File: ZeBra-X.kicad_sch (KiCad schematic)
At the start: 0 parts

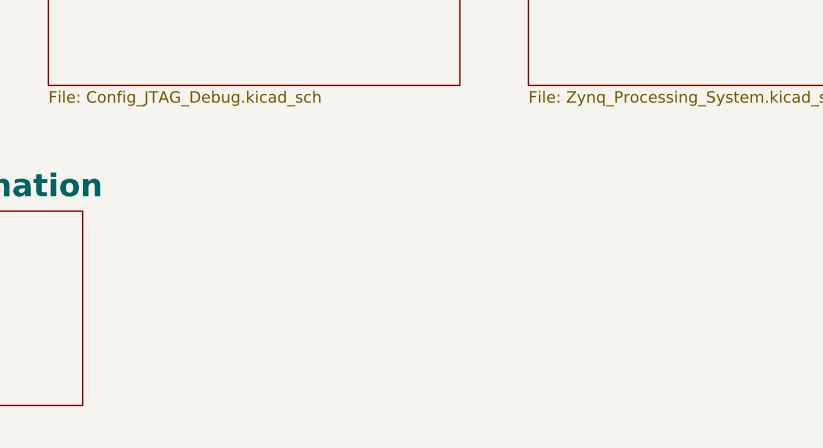
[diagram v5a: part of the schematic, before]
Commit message: Added page '[7] 1GB DDR3L Modules'
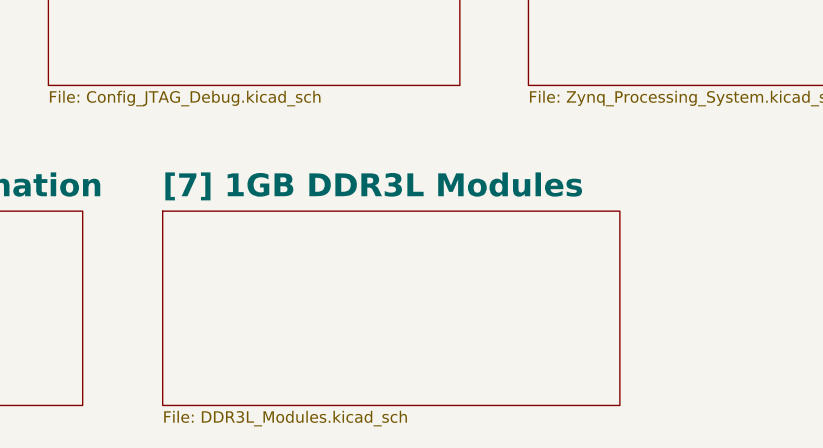
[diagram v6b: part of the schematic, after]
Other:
- added sheet [7] 1GB DDR3L Modules (DDR3L_Modules.kicad_sch)

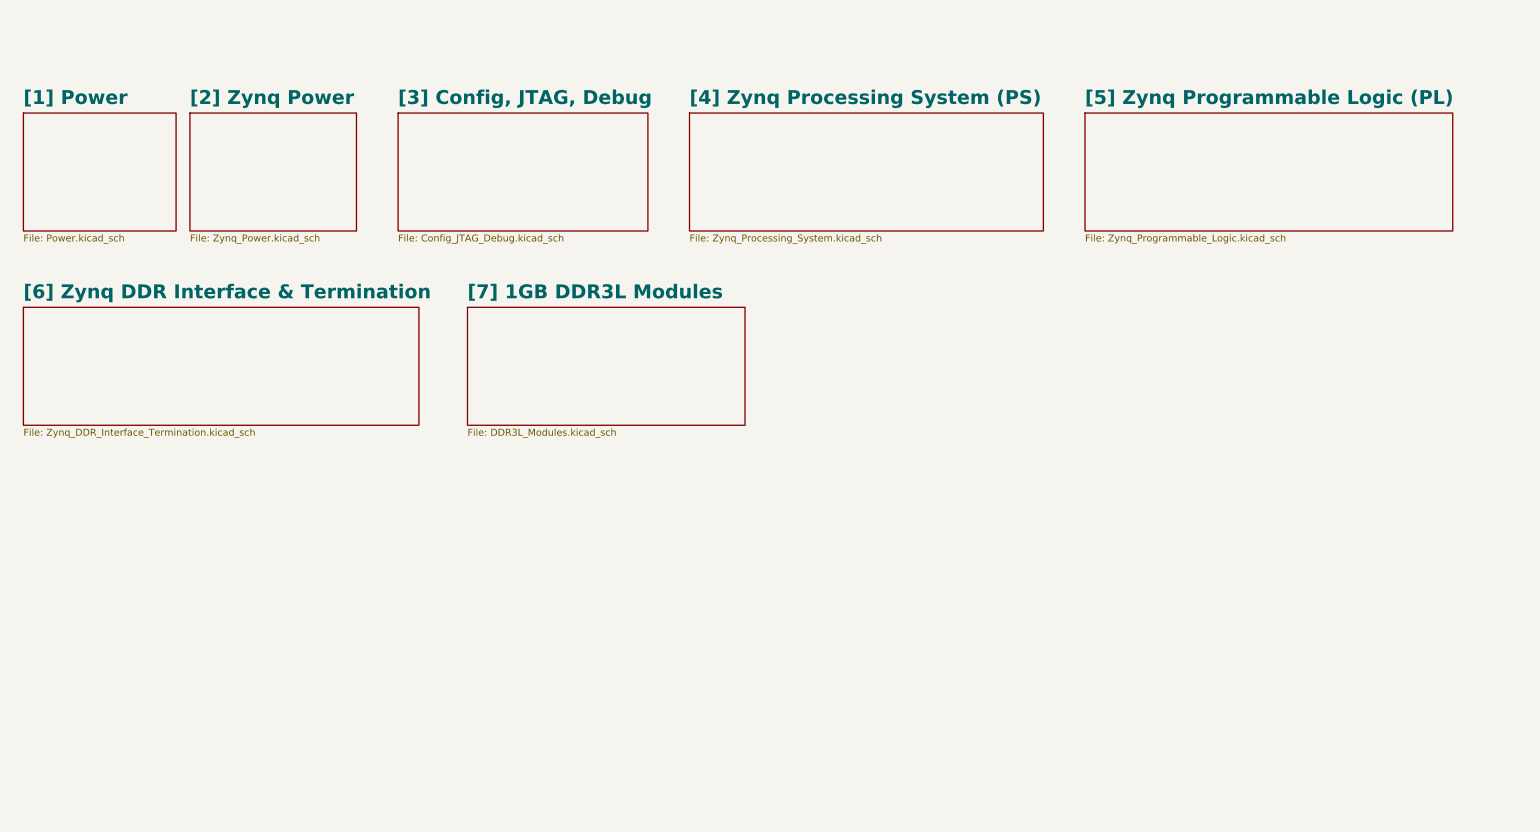
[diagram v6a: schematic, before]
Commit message: Added placeholders for sheets 8,9, and 10
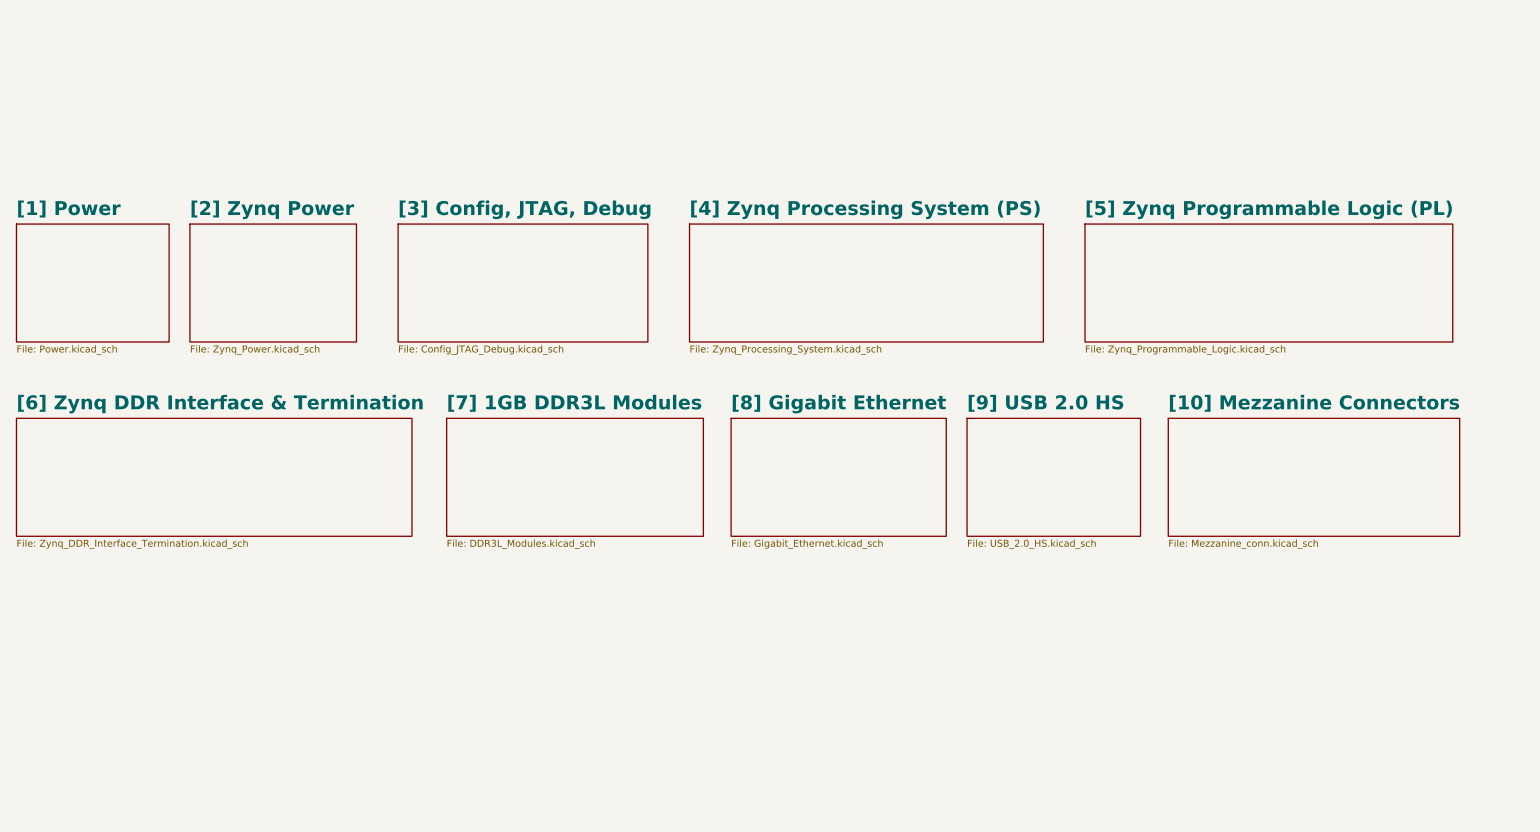
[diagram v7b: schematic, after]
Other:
- added sheet [10] Mezzanine Connectors (Mezzanine_conn.kicad_sch)
- added sheet [8] Gigabit Ethernet (Gigabit_Ethernet.kicad_sch)
- added sheet [9] USB 2.0 HS (USB_2.0_HS.kicad_sch)
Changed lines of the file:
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@@
 	)
 	(sheet
-		(at 138.43 33.02)
+		(at 138.43 53.34)
 		(size 64.77 21.59)
 		(fields_autoplaced yes)
@@
 		)
 		(property "Sheetname" "[4] Zynq Processing System (PS)"
-			(at 138.43 31.6734 0)
+			(at 138.43 51.9934 0)
 			(effects
 				(font
@@
 		)
 		(property "Sheetfile" "Zynq_Processing_System.kicad_sch"
-			(at 138.43 55.1946 0)
+			(at 138.43 75.5146 0)
 			(effects
 				(font
@@
 	)
 	(sheet
-		(at 97.79 68.58)
-		(size 50.8 21.59)
+		(at 93.98 88.9)
+		(size 46.99 21.59)
 		(fields_autoplaced yes)
 		(stroke
@@
 		)
 		(property "Sheetname" "[7] 1GB DDR3L Modules"
-			(at 97.79 67.2334 0)
+			(at 93.98 87.5534 0)
 			(effects
 				(font
@@
 		)
 		(property "Sheetfile" "DDR3L_Modules.kicad_sch"
-			(at 97.79 90.7546 0)
+			(at 93.98 111.0746 0)
 			(effects
 				(font
@@
 	)
 	(sheet
-		(at 210.82 33.02)
+		(at 210.82 53.34)
 		(size 67.31 21.59)
 		(fields_autoplaced yes)
@@
 		)
 		(property "Sheetname" "[5] Zynq Programmable Logic (PL)"
-			(at 210.82 31.6734 0)
+			(at 210.82 51.9934 0)
 			(effects
 				(font
@@
 		)
 		(property "Sheetfile" "Zynq_Programmable_Logic.kicad_sch"
-			(at 210.82 55.1946 0)
+			(at 210.82 75.5146 0)
 			(effects
 				(font
@@
 	)
 	(sheet
-		(at 16.51 68.58)
+		(at 15.24 88.9)
 		(size 72.39 21.59)
 		(fields_autoplaced yes)
@@
 		)
 		(property "Sheetname" "[6] Zynq DDR Interface & Termination"
-			(at 16.51 67.2334 0)
+			(at 15.24 87.5534 0)
 			(effects
 				(font
@@
 		)
 		(property "Sheetfile" "Zynq_DDR_Interface_Termination.kicad_sch"
-			(at 16.51 90.7546 0)
+			(at 15.24 111.0746 0)
 			(effects
 				(font
@@
 	)
 	(sheet
-		(at 46.99 33.02)
+		(at 146.05 88.9)
+		(size 39.37 21.59)
+		(fields_autoplaced yes)
+		(stroke
+			(width 0.1524)
+			(type solid)
+		)
+		(fill
+			(color 0 0 0 0.0000)
+		)
+		(property "Sheetname" "[8] Gigabit Ethernet"
+			(at 146.05 87.5534 0)
+			(effects
+				(font
+					(size 2.54 2.54)
+					(bold yes)
+				)
+				(justify left bottom)
+			)
+		)
+		(property "Sheetfile" "Gigabit_Ethernet.kicad_sch"
+			(at 146.05 111.0746 0)
+			(effects
+				(font
+					(size 1.27 1.27)
+				)
+				(justify left top)
+			)
+		)
+		(instances
+			(project "ZeBra-X"
+				(path "/ec71d28a-654e-4dfb-b412-dd09b7b3e4b8"
+					(page "9")
+				)
+			)
+		)
+	)
+	(sheet
+		(at 46.99 53.34)
 		(size 30.48 21.59)
 		(fields_autoplaced yes)
@@
 		)
 		(property "Sheetname" "[2] Zynq Power"
-			(at 46.99 31.6734 0)
+			(at 46.99 51.9934 0)
 			(effects
 				(font
@@
 		)
 		(property "Sheetfile" "Zynq_Power.kicad_sch"
-			(at 46.99 55.1946 0)
+			(at 46.99 75.5146 0)
 			(effects
 				(font
@@
 	)
 	(sheet
-		(at 85.09 33.02)
+		(at 226.06 88.9)
+		(size 53.34 21.59)
+		(fields_autoplaced yes)
+		(stroke
+			(width 0.1524)
+			(type solid)
+		)
+		(fill
+			(color 0 0 0 0.0000)
+		)
+		(property "Sheetname" "[10] Mezzanine Connectors"
+			(at 226.06 87.5534 0)
+			(effects
+				(font
+					(size 2.54 2.54)
+					(bold yes)
+				)
+				(justify left bottom)
+			)
+		)
+		(property "Sheetfile" "Mezzanine_conn.kicad_sch"
+			(at 226.06 111.0746 0)
+			(effects
+				(font
+					(size 1.27 1.27)
+				)
+				(justify left top)
+			)
+		)
+		(instances
+			(project "ZeBra-X"
+				(path "/ec71d28a-654e-4dfb-b412-dd09b7b3e4b8"
+					(page "11")
+				)
+			)
+		)
+	)
+	(sheet
+		(at 189.23 88.9)
+		(size 31.75 21.59)
+		(fields_autoplaced yes)
+		(stroke
+			(width 0.1524)
+			(type solid)
+		)
+		(fill
+			(color 0 0 0 0.0000)
+		)
+		(property "Sheetname" "[9] USB 2.0 HS"
+			(at 189.23 87.5534 0)
+			(effects
+				(font
+					(size 2.54 2.54)
+					(bold yes)
+				)
+				(justify left bottom)
+			)
+		)
+		(property "Sheetfile" "USB_2.0_HS.kicad_sch"
+			(at 189.23 111.0746 0)
+			(effects
+				(font
+					(size 1.27 1.27)
+				)
+				(justify left top)
+			)
+		)
+		(instances
+			(project "ZeBra-X"
+				(path "/ec71d28a-654e-4dfb-b412-dd09b7b3e4b8"
+					(page "10")
+				)
+			)
+		)
+	)
+	(sheet
+		(at 85.09 53.34)
 		(size 45.72 21.59)
 		(fields_autoplaced yes)
@@
 		)
 		(property "Sheetname" "[3] Config, JTAG, Debug"
-			(at 85.09 31.6734 0)
+			(at 85.09 51.9934 0)
 			(effects
 				(font
@@
 		)
 		(property "Sheetfile" "Config_JTAG_Debug.kicad_sch"
-			(at 85.09 55.1946 0)
+			(at 85.09 75.5146 0)
 			(effects
 				(font
@@
 	)
 	(sheet
-		(at 16.51 33.02)
+		(at 15.24 53.34)
 		(size 27.94 21.59)
 		(fields_autoplaced yes)
@@
 		)
 		(property "Sheetname" "[1] Power"
-			(at 16.51 31.6734 0)
+			(at 15.24 51.9934 0)
 			(effects
 				(font
@@
 		)
 		(property "Sheetfile" "Power.kicad_sch"
-			(at 16.51 55.1946 0)
-			(effects
-				(font
+			(at 15.24 75.5146 0)
+			(effects
+				(font

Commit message: Completed page 8, Gigabit Ethernet Controller
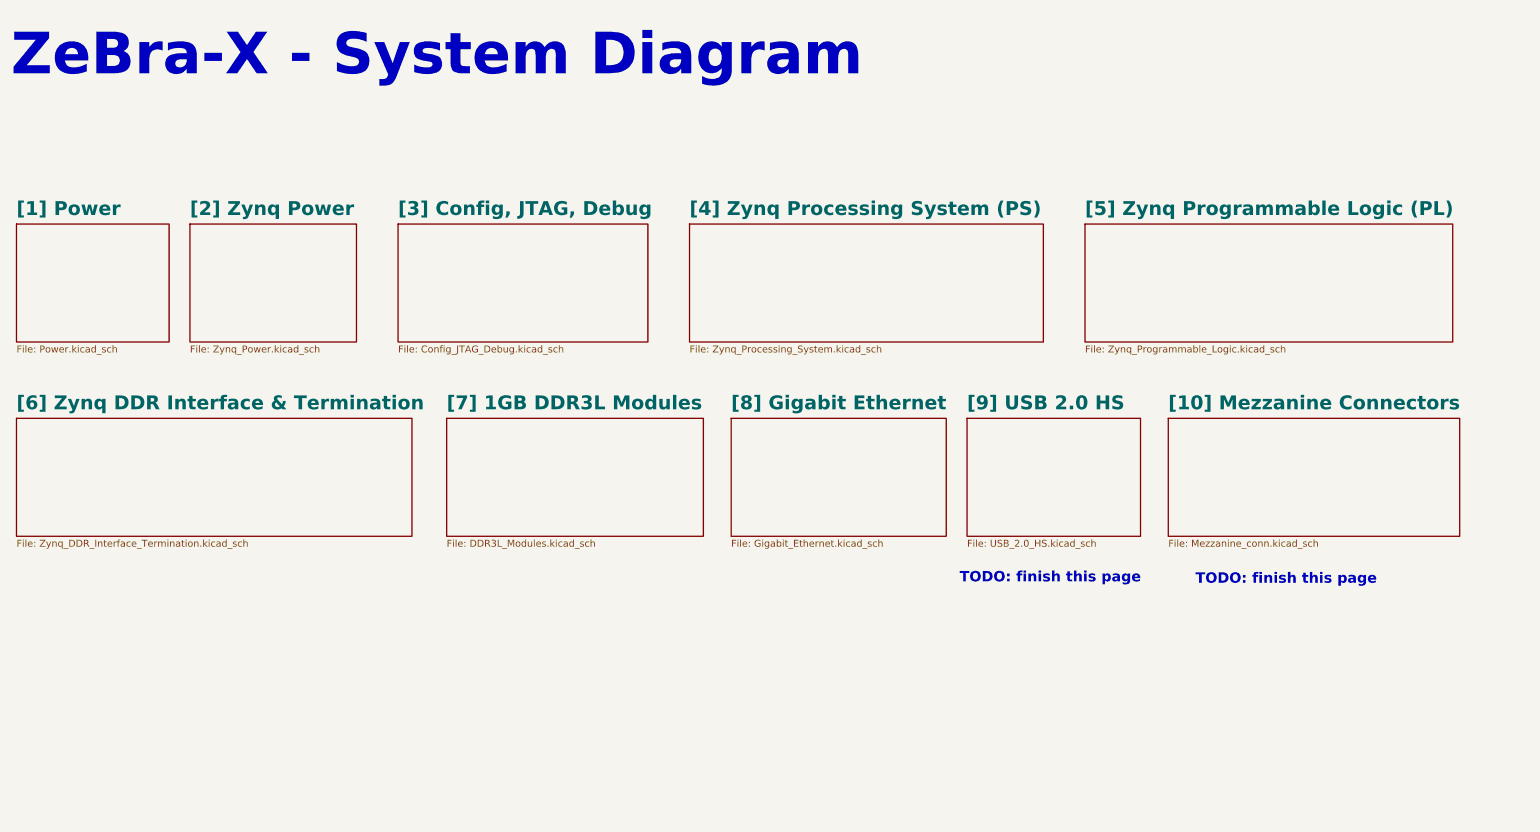
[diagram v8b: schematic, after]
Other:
- note added: "TODO: finish this page"
- note added: "ZeBra-X - System Diagram"
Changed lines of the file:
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@@
 		(comment 1 "Based on Phil's Lab \"ZettBrett\" board")
+	)
+	(text "ZeBra-X - System Diagram"
+		(exclude_from_sim no)
+		(at 14.224 26.924 0)
+		(effects
+			(font
+				(face "Century Gothic")
+				(size 7.62 7.62)
+				(thickness 1.016)
+				(bold yes)
+			)
+			(justify left bottom)
+		)
+	)
+	(text "TODO: finish this page"
+		(exclude_from_sim no)
+		(at 247.65 118.364 0)
+		(effects
+			(font
+				(size 1.905 1.905)
+				(thickness 0.381)
+				(bold yes)
+			)
+		)
+	)
+	(text "TODO: finish this page"
+		(exclude_from_sim no)
+		(at 204.47 118.11 0)
+		(effects
+			(font
+				(size 1.905 1.905)
+				(thickness 0.381)
+				(bold yes)
+			)
+		)
 	)
 	(sheet
